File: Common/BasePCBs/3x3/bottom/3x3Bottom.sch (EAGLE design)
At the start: 10 parts, among them CON1 SHIELD_FINGER0820, CON2 SHIELD_FINGER0820, CON3 SHIELD_FINGER0820, CON4 SHIELD_FINGER0820, CON5 SHIELD_FINGER0820, CON6 SHIELD_FINGER0820, CON7 SHIELD_FINGER0820, CON8 SHIELD_FINGER0820, CON9 SHIELD_FINGER0820

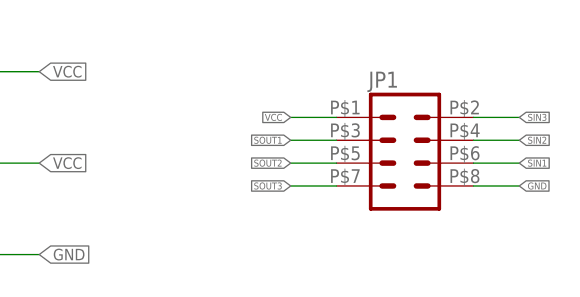
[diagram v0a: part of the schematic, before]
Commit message: fixed incorrect connections for the 3x3Bottom PCB
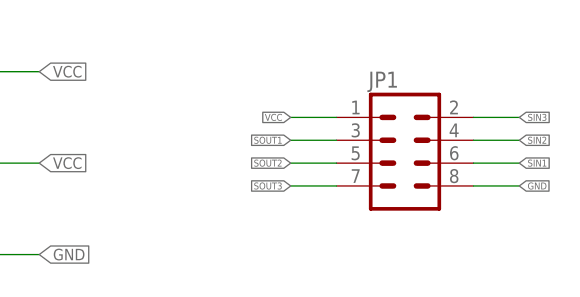
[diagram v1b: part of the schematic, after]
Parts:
- JP1: device MakerWear:M04X2 -> MakerWear:M04X2_0.1"
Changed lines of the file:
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@@
 <grid distance="0.1" unitdist="inch" unit="inch" style="lines" multiple="1" display="no" altdistance="0.01" altunitdist="inch" altunit="inch"/>
 <layers>
-<layer number="1" name="Top" color="4" fill="1" visible="no" active="no"/>
-<layer number="16" name="Bottom" color="1" fill="1" visible="no" active="no"/>
-<layer number="17" name="Pads" color="2" fill="1" visible="no" active="no"/>
-<layer number="18" name="Vias" color="2" fill="1" visible="no" active="no"/>
-<layer number="19" name="Unrouted" color="6" fill="1" visible="no" active="no"/>
-<layer number="20" name="Dimension" color="15" fill="1" visible="no" active="no"/>
-<layer number="21" name="tPlace" color="16" fill="1" visible="no" active="no"/>
-<layer number="22" name="bPlace" color="7" fill="1" visible="no" active="no"/>
-<layer number="23" name="tOrigins" color="15" fill="1" visible="no" active="no"/>
-<layer number="24" name="bOrigins" color="15" fill="1" visible="no" active="no"/>
-<layer number="25" name="tNames" color="7" fill="1" visible="no" active="no"/>
-<layer number="26" name="bNames" color="7" fill="1" visible="no" active="no"/>
-<layer number="27" name="tValues" color="7" fill="1" visible="no" active="no"/>
-<layer number="28" name="bValues" color="7" fill="1" visible="no" active="no"/>
+<layer number="1" name="Top" color="4" fill="1" visible="yes" active="no"/>
+<layer number="16" name="Bottom" color="1" fill="1" visible="yes" active="no"/>
+<layer number="17" name="Pads" color="2" fill="1" visible="yes" active="no"/>
+<layer number="18" name="Vias" color="2" fill="1" visible="yes" active="no"/>
+<layer number="19" name="Unrouted" color="6" fill="1" visible="yes" active="no"/>
+<layer number="20" name="Dimension" color="15" fill="1" visible="yes" active="no"/>
+<layer number="21" name="tPlace" color="7" fill="1" visible="yes" active="no"/>
+<layer number="22" name="bPlace" color="7" fill="1" visible="yes" active="no"/>
+<layer number="23" name="tOrigins" color="15" fill="1" visible="yes" active="no"/>
+<layer number="24" name="bOrigins" color="15" fill="1" visible="yes" active="no"/>
+<layer number="25" name="tNames" color="7" fill="1" visible="yes" active="no"/>
+<layer number="26" name="bNames" color="7" fill="1" visible="yes" active="no"/>
+<layer number="27" name="tValues" color="7" fill="1" visible="yes" active="no"/>
+<layer number="28" name="bValues" color="7" fill="1" visible="yes" active="no"/>
 <layer number="29" name="tStop" color="7" fill="3" visible="no" active="no"/>
 <layer number="30" name="bStop" color="7" fill="6" visible="no" active="no"/>
@@
 <layer number="35" name="tGlue" color="7" fill="4" visible="no" active="no"/>
 <layer number="36" name="bGlue" color="7" fill="5" visible="no" active="no"/>
-<layer number="37" name="tTest" color="7" fill="1" visible="no" active="no"/>
-<layer number="38" name="bTest" color="7" fill="1" visible="no" active="no"/>
+<layer number="37" name="tTest" color="7" fill="1" visible="yes" active="no"/>
+<layer number="38" name="bTest" color="7" fill="1" visible="yes" active="no"/>
 <layer number="39" name="tKeepout" color="4" fill="11" visible="no" active="no"/>
 <layer number="40" name="bKeepout" color="1" fill="11" visible="no" active="no"/>
@@
 <layer number="44" name="Drills" color="7" fill="1" visible="no" active="no"/>
 <layer number="45" name="Holes" color="7" fill="1" visible="no" active="no"/>
-<layer number="46" name="Milling" color="3" fill="1" visible="no" active="no"/>
-<layer number="47" name="Measures" color="7" fill="1" visible="no" active="no"/>
-<layer number="48" name="Document" color="7" fill="1" visible="no" active="no"/>
-<layer number="49" name="Reference" color="7" fill="1" visible="no" active="no"/>
-<layer number="50" name="dxf" color="7" fill="1" visible="no" active="no"/>
-<layer number="51" name="tDocu" color="14" fill="1" visible="no" active="no"/>
-<layer number="52" name="bDocu" color="7" fill="1" visible="no" active="no"/>
-<layer number="53" name="tGND_GNDA" color="7" fill="9" visible="no" active="no"/>
-<layer number="54" name="bGND_GNDA" color="1" fill="9" visible="no" active="no"/>
-<layer number="56" name="wert" color="7" fill="1" visible="no" active="no"/>
-<layer number="57" name="tCAD" color="7" fill="1" visible="no" active="no"/>
-<layer number="59" name="tCarbon" color="7" fill="1" visible="no" active="no"/>
-<layer number="60" name="bCarbon" color="7" fill="1" visible="no" active="no"/>
+<layer number="46" name="Milling" color="3" fill="1" visible="yes" active="no"/>
+<layer number="47" name="Measures" color="7" fill="1" visible="yes" active="no"/>
+<layer number="48" name="Document" color="7" fill="1" visible="yes" active="no"/>
+<layer number="49" name="Reference" color="7" fill="1" visible="yes" active="no"/>
+<layer number="50" name="dxf" color="7" fill="1" visible="yes" active="no"/>
+<layer number="51" name="tDocu" color="7" fill="1" visible="yes" active="no"/>
+<layer number="52" name="bDocu" color="7" fill="1" visible="yes" active="no"/>
+<layer number="53" name="tGND_GNDA" color="7" fill="9" visible="yes" active="no"/>
+<layer number="54" name="bGND_GNDA" color="1" fill="9" visible="yes" active="no"/>
+<layer number="56" name="wert" color="7" fill="1" visible="yes" active="no"/>
+<layer number="57" name="tCAD" color="7" fill="1" visible="yes" active="no"/>
+<layer number="59" name="tCarbon" color="7" fill="1" visible="yes" active="no"/>
+<layer number="60" name="bCarbon" color="7" fill="1" visible="yes" active="no"/>
 <layer number="90" name="Modules" color="5" fill="1" visible="yes" active="yes"/>
 <layer number="91" name="Nets" color="2" fill="1" visible="yes" active="yes"/>
@@
 <part name="CON9" library="MakerShoe" deviceset="SHIELD_FINGER" device="0820"/>
 <part name="CON1" library="MakerShoe" deviceset="SHIELD_FINGER" device="0820"/>
-<part name="JP1" library="MakerWear" deviceset="M04X2" device=""/>
+<part name="JP1" library="MakerWear" deviceset="M04X2_0.1&quot;" device=""/>
 </parts>
 <sheets>
